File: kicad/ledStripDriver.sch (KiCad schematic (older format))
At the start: 33 parts, among them J1 AudioJack3_SwitchTR, K1 G5RL1AELN5DC, Q1 Q_NPN_BEC_S8050, Q2 AO3400, Q3 AO3400, Q4 AO3400, SW1 SW_DIP_x01, SW2 Rotary_Encoder_Switch, SW3 SW_Push, U1 MOD_ESP32_DEV_universal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

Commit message: KiCad fixes: flip Jack, add resistor on 12V logic to protect LEDs.
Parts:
- added R10, R8, R9: 300ohm, Resistor_SMD:R_0805_2012Metric_Pad1.15x1.40mm_HandSolder, symbol Device:R
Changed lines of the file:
@@
 Wire Wire Line
 	10400 1250 10350 1250
-Wire Wire Line
-	10400 1250 10700 1250
 Connection ~ 10400 1250
 Wire Wire Line
@@
 Wire Wire Line
 	9750 1250 9950 1250
-Text Label 10400 1250 0    50   ~ 0
+Text Label 10700 1250 0    50   ~ 0
 STRIP1_LOGIC_12V
 $Comp
@@
 Wire Wire Line
 	10400 2200 10350 2200
-Wire Wire Line
-	10400 2200 10700 2200
 Connection ~ 10400 2200
 Wire Wire Line
@@
 Wire Wire Line
 	9750 2200 9950 2200
-Text Label 10400 2200 0    50   ~ 0
-STRIP2_LOGIC_12V
 $Comp
 L power:+3V3 #PWR0114
@@
 P 10400 2950
 F 0 "R7" H 10470 2996 50  0000 L CNN
-F 1 "5kOhm" H 10470 2905 50  0000 L CNN
+F 1 "5kOhm" H 10400 3100 50  0000 L CNN
 F 2 "Resistor_SMD:R_0805_2012Metric_Pad1.15x1.40mm_HandSolder" V 10330 2950 50  0001 C CNN
 F 3 "~" H 10400 2950 50  0001 C CNN
@@
 	10400 3200 10350 3200
 Wire Wire Line
-	10400 3200 10700 3200
-Connection ~ 10400 3200
-Wire Wire Line
 	9550 3200 9750 3200
 Wire Wire Line
@@
 Wire Wire Line
 	9750 3200 9950 3200
-Text Label 10400 3200 0    50   ~ 0
+Text Label 10750 3200 0    50   ~ 0
 STRIP3_LOGIC_12V
 Text Label 9550 1250 2    50   ~ 0
@@
 Wire Wire Line
 	2600 4250 2650 4250
+$Comp
+L Device:R R10
+U 1 1 5E7C1E56
+P 10550 3200
+F 0 "R10" V 10550 3200 50  0000 C CNN
+F 1 "300ohm" V 10450 3150 50  0000 C CNN
+F 2 "Resistor_SMD:R_0805_2012Metric_Pad1.15x1.40mm_HandSolder" V 10480 3200 50  0001 C CNN
+F 3 "~" H 10550 3200 50  0001 C CNN
+	1    10550 3200
+	0    -1   -1   0
+$EndComp
+Connection ~ 10400 3200
+Wire Wire Line
+	11050 3200 10700 3200
+$Comp
+L Device:R R9
+U 1 1 5E7F5FB9
+P 10550 2200
+F 0 "R9" V 10550 2200 50  0000 C CNN
+F 1 "300ohm" V 10450 2200 50  0000 C CNN
+F 2 "Resistor_SMD:R_0805_2012Metric_Pad1.15x1.40mm_HandSolder" V 10480 2200 50  0001 C CNN
+F 3 "~" H 10550 2200 50  0001 C CNN
+	1    10550 2200
+	0    -1   -1   0
+$EndComp
+Wire Wire Line
+	10700 2200 11100 2200
+$Comp
+L Device:R R8
+U 1 1 5E7F63B4
+P 10550 1250
+F 0 "R8" V 10550 1250 50  0000 C CNN
+F 1 "300ohm" V 10450 1250 50  0000 C CNN
+F 2 "Resistor_SMD:R_0805_2012Metric_Pad1.15x1.40mm_HandSolder" V 10480 1250 50  0001 C CNN
+F 3 "~" H 10550 1250 50  0001 C CNN
+	1    10550 1250
+	0    -1   -1   0
+$EndComp
+Wire Wire Line
+	10700 1250 11100 1250
+Text Label 10750 2200 0    50   ~ 0
+STRIP2_LOGIC_12V
 $EndSCHEMATC

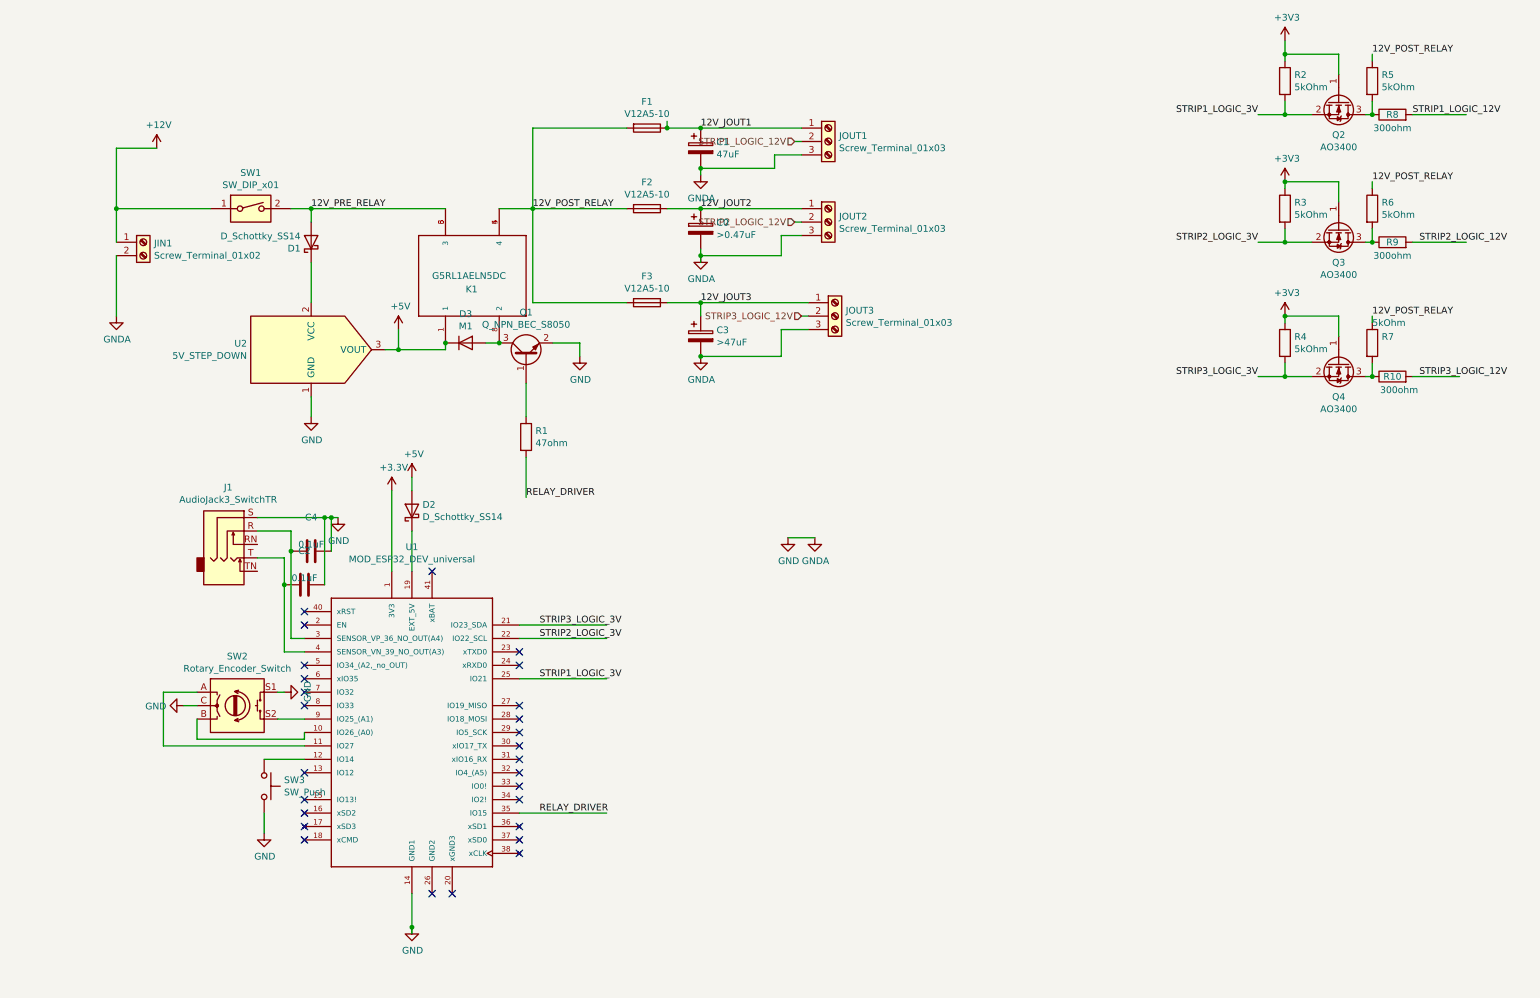
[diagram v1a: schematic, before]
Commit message: Modified schema to consiste MSQ spectrum analyzer. No PCB updates yet.
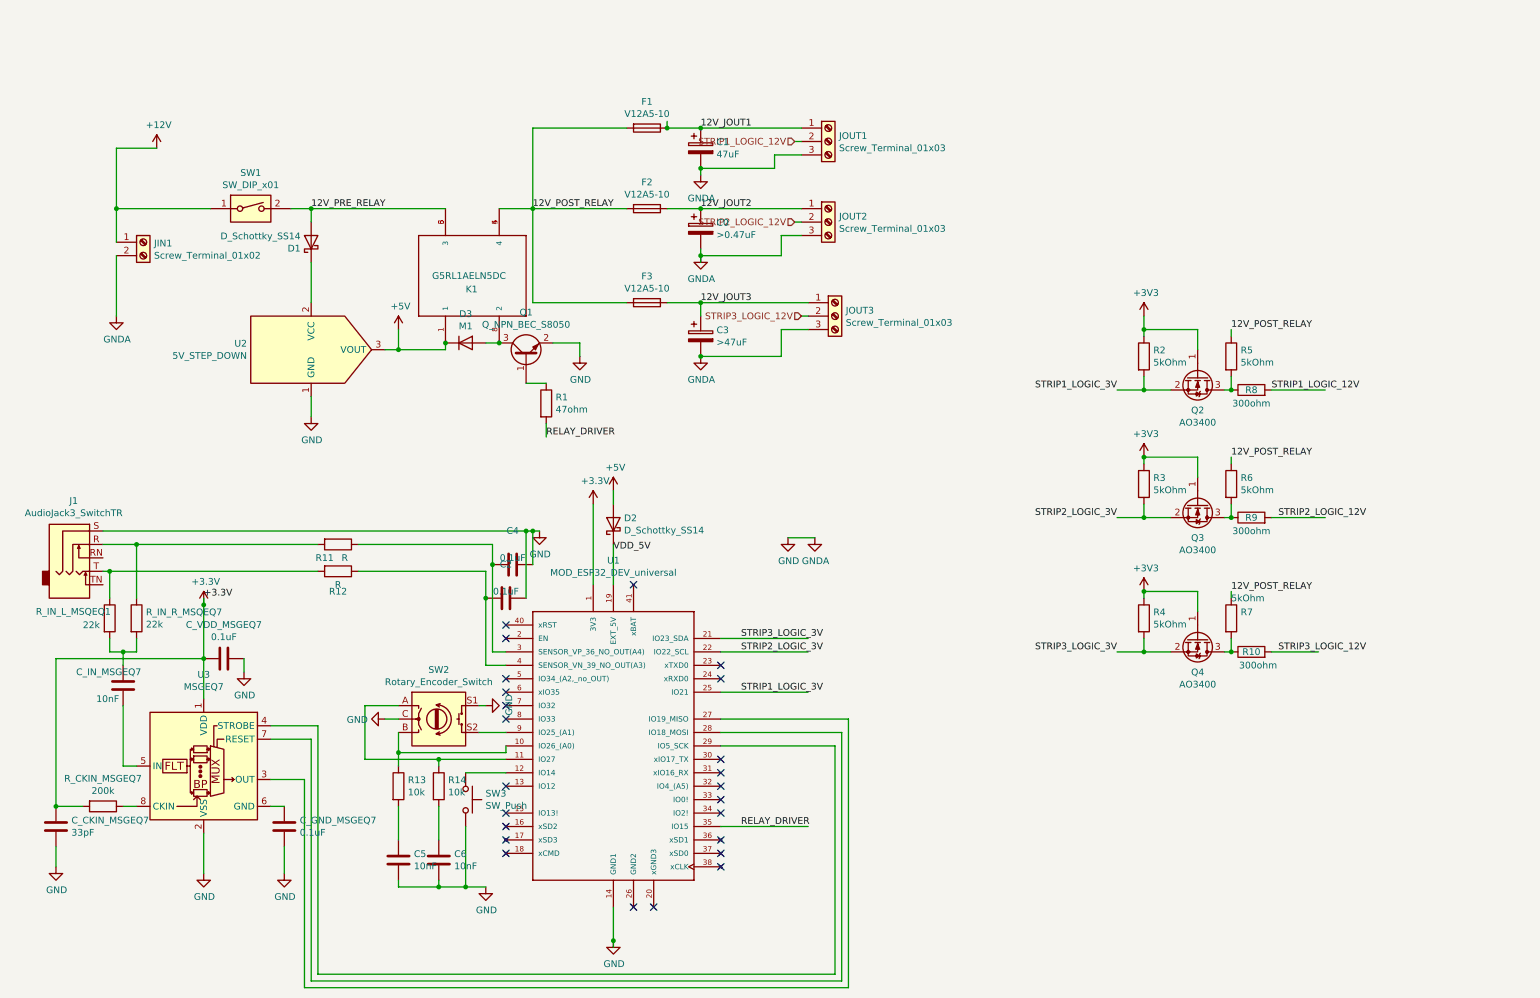
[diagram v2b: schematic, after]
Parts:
- added C5, C6, C_IN_MSGEQ7: 10nF, Capacitor_SMD:C_0805_2012Metric_Pad1.15x1.40mm_HandSolder, symbol Device:C
- added C_CKIN_MSGEQ7: 33pF, Capacitor_SMD:C_0805_2012Metric_Pad1.15x1.40mm_HandSolder, symbol Device:C
- added C_GND_MSGEQ7, C_VDD_MSGEQ7: 0.1uF, Capacitor_SMD:C_0805_2012Metric_Pad1.15x1.40mm_HandSolder, symbol Device:C
- added R11, R12: R, Resistor_SMD:R_0805_2012Metric_Pad1.15x1.40mm_HandSolder, symbol Device:R
- added R13, R14: 10k, Resistor_SMD:R_0805_2012Metric_Pad1.15x1.40mm_HandSolder, symbol Device:R
- added R_CKIN_MSGEQ7: 200k, Resistor_SMD:R_0805_2012Metric_Pad1.15x1.40mm_HandSolder, symbol Device:R
- added R_IN_L_MSQEQ1, R_IN_R_MSQEQ7: 22k, Resistor_SMD:R_0805_2012Metric_Pad1.15x1.40mm_HandSolder, symbol Device:R
- added U3: MSGEQ7, Package_DIP:DIP-8_W7.62mm_Socket, symbol Audio:MSGEQ7
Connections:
- net labels added: VDD_5V
- wire segments 113 -> 163
- no-connect marks 27 -> 24
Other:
- moved on the sheet: C2, C4, D2, J1, Q2, Q3, Q4, R1, R10, R2, R3, R4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

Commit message: Refreshed PCB and footprints of (Fuse holder, Rocker switch, Screw-terminal for input)
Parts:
- F1, F2, F3: footprint ptabOther:FUSE_HOLDER_CAR_MEDIUM_PA66 -> Fuse:Fuseholder_Cylinder-5x20mm_Schurter_0031_8201_Horizontal_Open
- JIN1: footprint TerminalBlock_RND:TerminalBlock_RND_205-00023_1x02_P10.00mm_Horizontal -> ptabOther:TerminalBlock_RND_205-00023_1x02_P10.00mm_Horizontal(2mmdrill)
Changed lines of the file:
@@
 F 0 "JIN1" H 1330 2192 50  0000 L CNN
 F 1 "Screw_Terminal_01x02" H 1330 2101 50  0000 L CNN
-F 2 "TerminalBlock_RND:TerminalBlock_RND_205-00023_1x02_P10.00mm_Horizontal" H 1250 2200 50  0001 C CNN
+F 2 "ptabOther:TerminalBlock_RND_205-00023_1x02_P10.00mm_Horizontal(2mmdrill)" H 1250 2200 50  0001 C CNN
 F 3 "~" H 1250 2200 50  0001 C CNN
 	1    1250 2200
@@
 F 0 "F2" V 4803 1950 50  0000 C CNN
 F 1 "V12A5-10" V 4894 1950 50  0000 C CNN
-F 2 "ptabOther:FUSE_HOLDER_CAR_MEDIUM_PA66" V 4930 1950 50  0001 C CNN
+F 2 "Fuse:Fuseholder_Cylinder-5x20mm_Schurter_0031_8201_Horizontal_Open" V 4930 1950 50  0001 C CNN
 F 3 "~" H 5000 1950 50  0001 C CNN
 	1    5000 1950
@@
 F 0 "F1" V 4803 1350 50  0000 C CNN
 F 1 "V12A5-10" V 4894 1350 50  0000 C CNN
-F 2 "ptabOther:FUSE_HOLDER_CAR_MEDIUM_PA66" V 4930 1350 50  0001 C CNN
+F 2 "Fuse:Fuseholder_Cylinder-5x20mm_Schurter_0031_8201_Horizontal_Open" V 4930 1350 50  0001 C CNN
 F 3 "~" H 5000 1350 50  0001 C CNN
 	1    5000 1350
@@
 F 0 "F3" V 4803 2650 50  0000 C CNN
 F 1 "V12A5-10" V 4894 2650 50  0000 C CNN
-F 2 "ptabOther:FUSE_HOLDER_CAR_MEDIUM_PA66" V 4930 2650 50  0001 C CNN
+F 2 "Fuse:Fuseholder_Cylinder-5x20mm_Schurter_0031_8201_Horizontal_Open" V 4930 2650 50  0001 C CNN
 F 3 "~" H 5000 2650 50  0001 C CNN
 	1    5000 2650

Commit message: PCB v2 - with hardware spectrum analyzer.
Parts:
- F1, F2, F3: footprint Fuse:Fuseholder_Cylinder-5x20mm_Schurter_0031_8201_Horizontal_Open -> Fuse:Fuseholder_Cylinder-5x20mm_Stelvio-Kontek_PTF78_Horizontal_Open
- SW1: footprint ptabOther:ROCKER_SWITCH -> ptabOther:ROCKER_SWITCH_7x0.5mm
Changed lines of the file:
@@
 F 0 "SW1" H 2050 2217 50  0000 C CNN
 F 1 "SW_DIP_x01" H 2050 2126 50  0000 C CNN
-F 2 "ptabOther:ROCKER_SWITCH" H 2050 1950 50  0001 C CNN
+F 2 "ptabOther:ROCKER_SWITCH_7x0.5mm" H 2050 1950 50  0001 C CNN
 F 3 "~" H 2050 1950 50  0001 C CNN
 	1    2050 1950
@@
 F 0 "F2" V 4803 1950 50  0000 C CNN
 F 1 "V12A5-10" V 4894 1950 50  0000 C CNN
-F 2 "Fuse:Fuseholder_Cylinder-5x20mm_Schurter_0031_8201_Horizontal_Open" V 4930 1950 50  0001 C CNN
+F 2 "Fuse:Fuseholder_Cylinder-5x20mm_Stelvio-Kontek_PTF78_Horizontal_Open" V 4930 1950 50  0001 C CNN
 F 3 "~" H 5000 1950 50  0001 C CNN
 	1    5000 1950
@@
 F 0 "F1" V 4803 1350 50  0000 C CNN
 F 1 "V12A5-10" V 4894 1350 50  0000 C CNN
-F 2 "Fuse:Fuseholder_Cylinder-5x20mm_Schurter_0031_8201_Horizontal_Open" V 4930 1350 50  0001 C CNN
+F 2 "Fuse:Fuseholder_Cylinder-5x20mm_Stelvio-Kontek_PTF78_Horizontal_Open" V 4930 1350 50  0001 C CNN
 F 3 "~" H 5000 1350 50  0001 C CNN
 	1    5000 1350
@@
 F 0 "F3" V 4803 2650 50  0000 C CNN
 F 1 "V12A5-10" V 4894 2650 50  0000 C CNN
-F 2 "Fuse:Fuseholder_Cylinder-5x20mm_Schurter_0031_8201_Horizontal_Open" V 4930 2650 50  0001 C CNN
+F 2 "Fuse:Fuseholder_Cylinder-5x20mm_Stelvio-Kontek_PTF78_Horizontal_Open" V 4930 2650 50  0001 C CNN
 F 3 "~" H 5000 2650 50  0001 C CNN
 	1    5000 2650

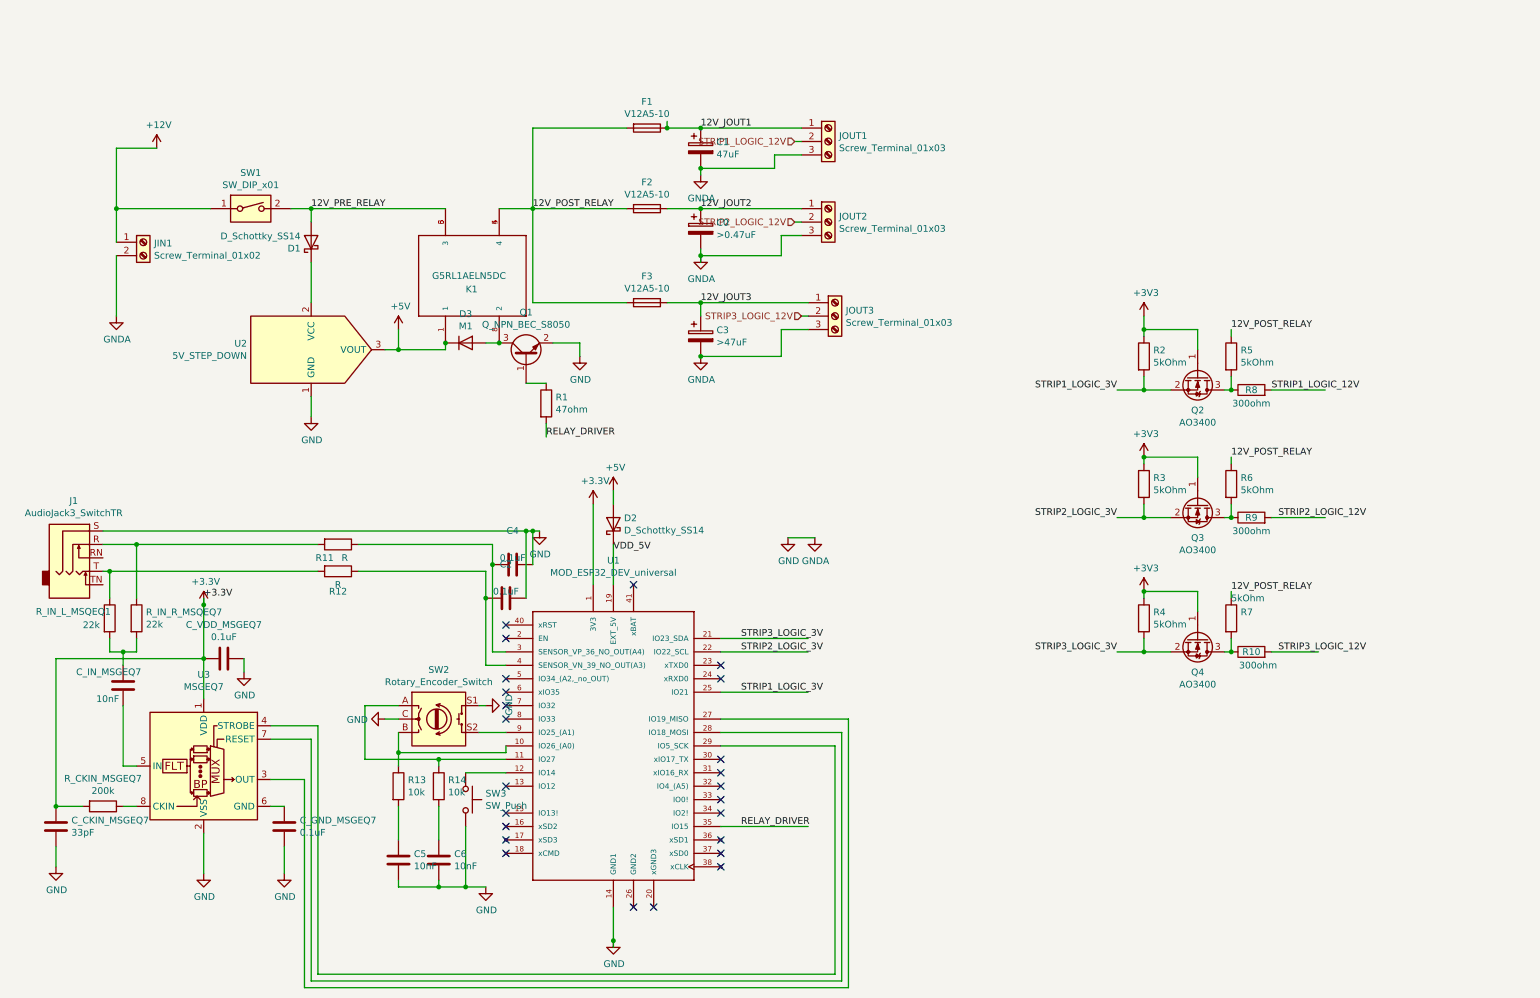
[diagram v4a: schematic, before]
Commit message: PCB v3: Hopefully manufacturing ready.
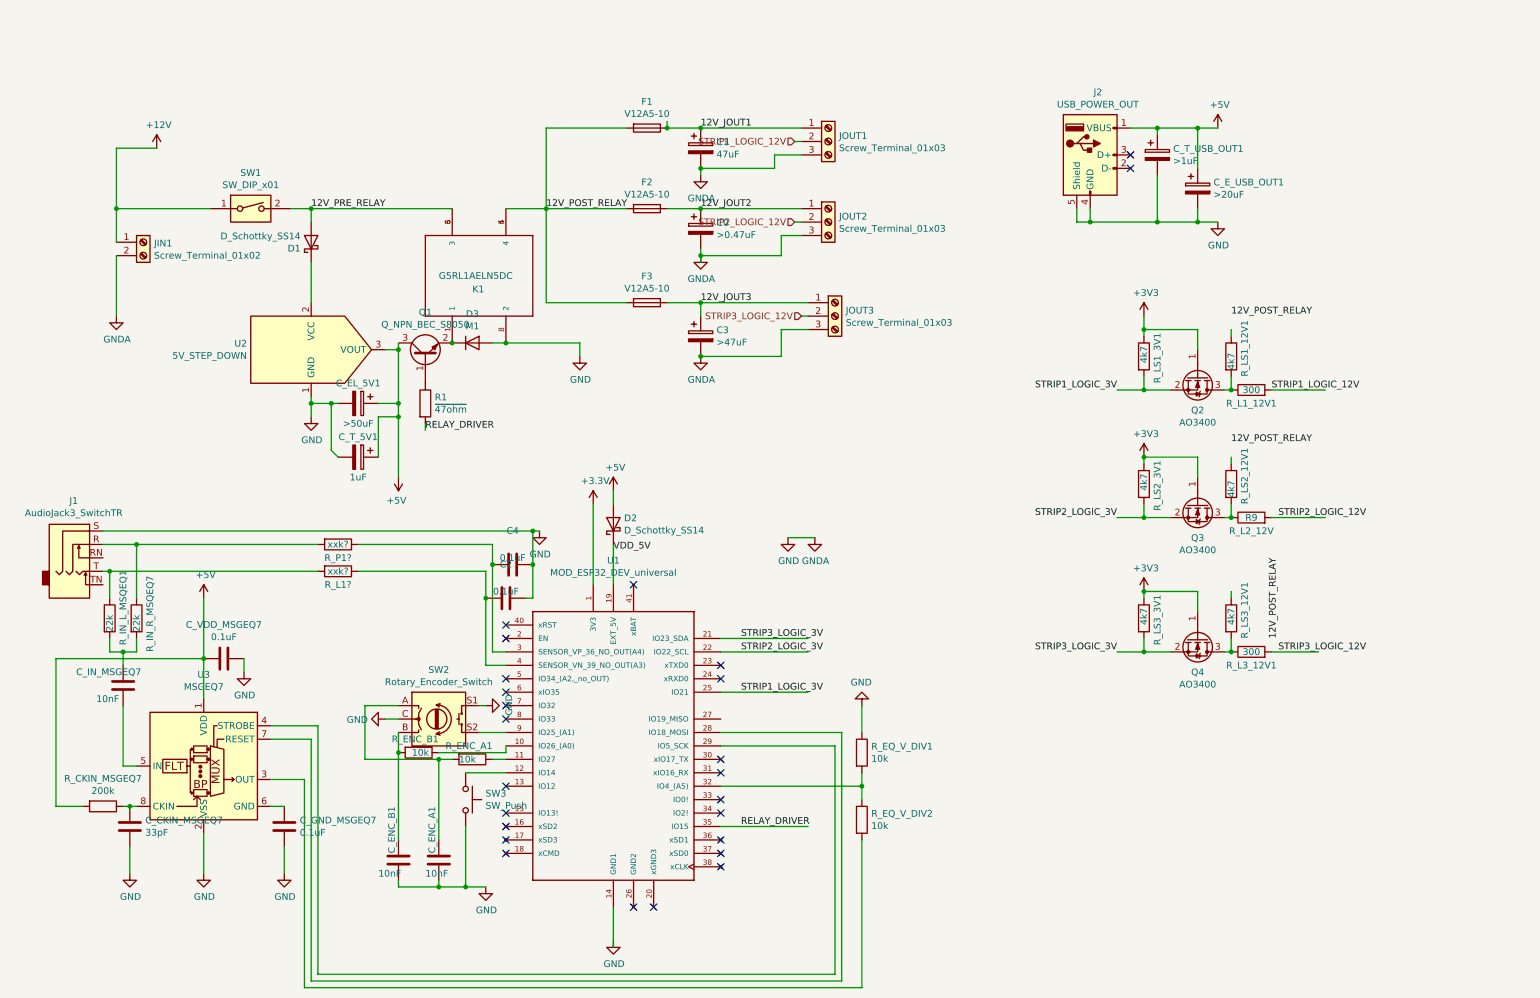
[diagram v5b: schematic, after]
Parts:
- added C_EL_5V1: >50uF, Capacitor_SMD:CP_Elec_6.3x5.4, symbol Device:CP
- added C_E_USB_OUT1: >20uF, Capacitor_SMD:CP_Elec_6.3x5.4, symbol Device:CP
- added C_T_5V1: 1uF, Capacitor_SMD:C_0805_2012Metric_Pad1.15x1.40mm_HandSolder, symbol Device:CP
- added C_T_USB_OUT1: >1uF, Capacitor_SMD:C_0805_2012Metric_Pad1.15x1.40mm_HandSolder, symbol Device:CP
- added J2: USB_POWER_OUT, Connector_USB:USB_A_CONNFLY_DS1095-WNR0, symbol Connector:USB_A
- added R_EQ_V_DIV1, R_EQ_V_DIV2: 10k, Resistor_SMD:R_0805_2012Metric_Pad1.15x1.40mm_HandSolder, symbol Device:R
- R1: value 47ohm -> ~47ohm
- R9: value 300ohm -> R_L2_12V
- R_L1?: renamed from R12; value R -> xxk?
- R_L1_12V1: renamed from R8; value 300ohm -> 300
- R_L3_12V1: renamed from R10; value 300ohm -> 300
- R_LS1_12V1: renamed from R5; value 5kOhm -> 4k7
- R_LS1_3V1: renamed from R2; value 5kOhm -> 4k7
- R_LS2_12V1: renamed from R6; value 5kOhm -> 4k7
- R_LS2_3V1: renamed from R3; value 5kOhm -> 4k7
- R_LS3_12V1: renamed from R7; value 5kOhm -> 4k7
- R_LS3_3V1: renamed from R4; value 5kOhm -> 4k7
- R_P1?: renamed from R11; value R -> xxk?
- renumbered C6 to C_ENC_A1, C5 to C_ENC_B1, R14 to R_ENC_A1, R13 to R_ENC_B1
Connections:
- wire segments 163 -> 185
- no-connect marks 24 -> 25
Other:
- moved on the sheet: C_CKIN_MSGEQ7, D3, K1, Q1, R1, R_ENC_A1, R_ENC_B1
